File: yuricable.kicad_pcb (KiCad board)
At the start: 2 copper layers, 66 x 25.4 mm, 24 parts, among them U1 FlipperZero

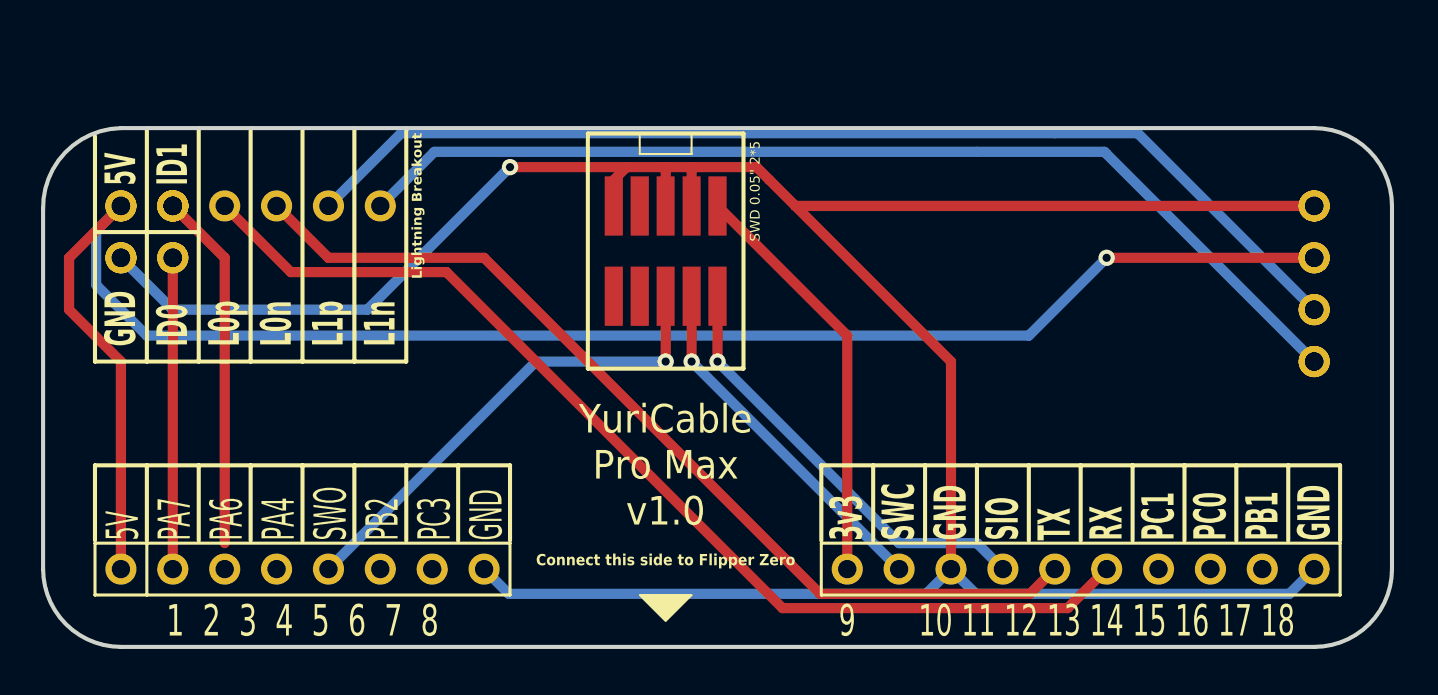
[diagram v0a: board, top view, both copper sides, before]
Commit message: some more markers on silkscreen
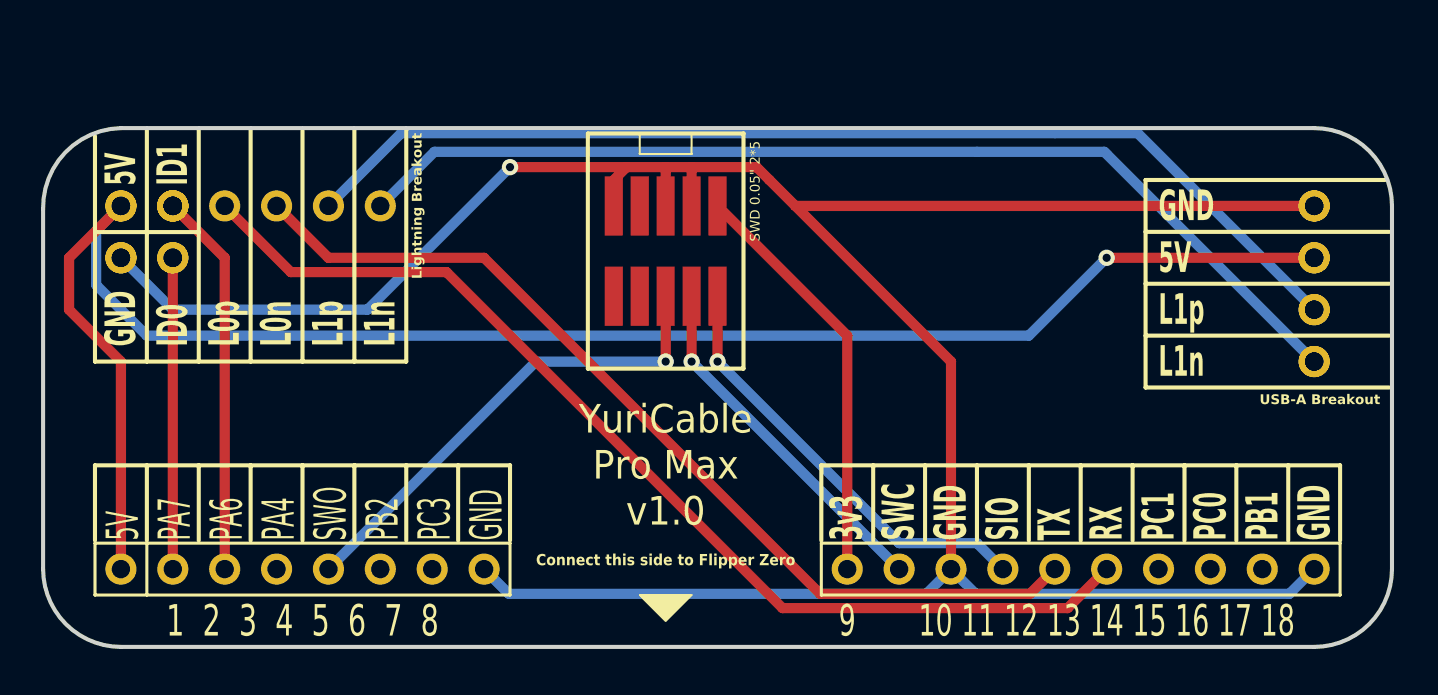
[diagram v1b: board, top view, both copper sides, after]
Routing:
- net /PA6: track 17.6 -> 18.8 mm
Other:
- board text added: "USB-A Breakout"
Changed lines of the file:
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@@
     (grid_origin 91.44 63.5)
     (pcbplotparams
-      (layerselection 0x00010fc_ffffffff)
+      (layerselection 0x003ffff_ffffffff)
       (plot_on_all_layers_selection 0x0000000_00000000)
       (disableapertmacros false)
@@
       (drillshape 0)
       (scaleselection 1)
-      (outputdirectory "gerbers")
+      (outputdirectory "/Users/antonstadie/Developer/KiCAD/yuricable-pcb-kicad/gerber")
     )
   )
@@
   (gr_line (start 62.23 71.12) (end 62.23 74.8)
     (stroke (width 0.2) (type solid)) (layer "F.SilkS"))
+  (gr_line (start 113.665 62.23) (end 125.6 62.23)
+    (stroke (width 0.2) (type solid)) (layer "F.SilkS"))
+  (gr_line (start 113.665 67.31) (end 125.6 67.31)
+    (stroke (width 0.2) (type solid)) (layer "F.SilkS"))
   (gr_line (start 115.57 71.12) (end 115.57 74.8)
     (stroke (width 0.2) (type solid)) (layer "F.SilkS"))
@@
   (gr_line (start 97.79 71.12) (end 97.79 74.8)
     (stroke (width 0.2) (type solid)) (layer "F.SilkS"))
+  (gr_line (start 113.665 64.77) (end 125.6 64.77)
+    (stroke (width 0.2) (type solid)) (layer "F.SilkS"))
   (gr_line (start 64.77 71.12) (end 64.77 74.8)
     (stroke (width 0.2) (type solid)) (layer "F.SilkS"))
@@
     (stroke (width 0.2) (type solid)) (layer "F.SilkS"))
   (gr_line (start 107.95 71.12) (end 107.95 74.8)
+    (stroke (width 0.2) (type solid)) (layer "F.SilkS"))
+  (gr_line (start 113.665 67.31) (end 113.665 57.15)
     (stroke (width 0.2) (type solid)) (layer "F.SilkS"))
   (gr_line (start 118.11 71.12) (end 118.11 74.8)
@@
     )
     (stroke (width 0.1) (type solid)) (fill solid) (layer "F.SilkS"))
+  (gr_line (start 113.665 59.69) (end 125.6 59.69)
+    (stroke (width 0.2) (type solid)) (layer "F.SilkS"))
   (gr_line (start 62.23 59.7) (end 67.31 59.7)
     (stroke (width 0.2) (type solid)) (layer "F.SilkS"))
   (gr_line (start 110.49 71.12) (end 110.49 74.8)
+    (stroke (width 0.2) (type solid)) (layer "F.SilkS"))
+  (gr_line (start 113.665 57.15) (end 125.4 57.15)
     (stroke (width 0.2) (type solid)) (layer "F.SilkS"))
   (gr_line (start 62.23 55) (end 62.23 66.04)
@@
     (effects (font (size 1.5 0.8) (thickness 0.2) bold) (justify left))
   )
+  (gr_text "5V" (at 114.3 60.96) (layer "F.SilkS")
+    (effects (font (size 1.5 0.8) (thickness 0.2) bold) (justify left))
+  )
   (gr_text "Connect this side to Flipper Zero\n\n" (at 90.17 76.2) (layer "F.SilkS")
     (effects (font (size 0.55 0.5) (thickness 0.12) bold))
   )
+  (gr_text "GND" (at 114.3 58.42) (layer "F.SilkS")
+    (effects (font (size 1.5 0.8) (thickness 0.2) bold) (justify left))
+  )
   (gr_text "L1p\n" (at 73.66 65.3 90) (layer "F.SilkS")
+    (effects (font (size 1.5 0.8) (thickness 0.2) bold) (justify left))
+  )
+  (gr_text "L1n" (at 114.3 66.04) (layer "F.SilkS")
     (effects (font (size 1.5 0.8) (thickness 0.2) bold) (justify left))
   )
@@
     (effects (font (size 1.5 0.8) (thickness 0.2) bold) (justify left))
   )
+  (gr_text "USB-A Breakout" (at 122.2 67.9) (layer "F.SilkS")
+    (effects (font (size 0.48 0.48) (thickness 0.12) bold))
+  )
   (gr_text "L0n\n" (at 71.12 65.3 90) (layer "F.SilkS")
+    (effects (font (size 1.5 0.8) (thickness 0.2) bold) (justify left))
+  )
+  (gr_text "L1p" (at 114.3 63.5) (layer "F.SilkS")
     (effects (font (size 1.5 0.8) (thickness 0.2) bold) (justify left))
   )
@@
   (segment (start 83.82 66.04) (end 90.17 66.04) (width 0.5) (layer "B.Cu") (net 13))
   (segment (start 68.58 60.96) (end 66.04 58.42) (width 0.5) (layer "F.Cu") (net 15))
-  (segment (start 68.58 74.93) (end 68.58 60.96) (width 0.5) (layer "F.Cu") (net 15))
+  (segment (start 68.58 60.96) (end 68.58 76.2) (width 0.5) (layer "F.Cu") (net 15))
   (segment (start 66.04 76.2) (end 66.04 60.96) (width 0.5) (layer "F.Cu") (net 16))
 )

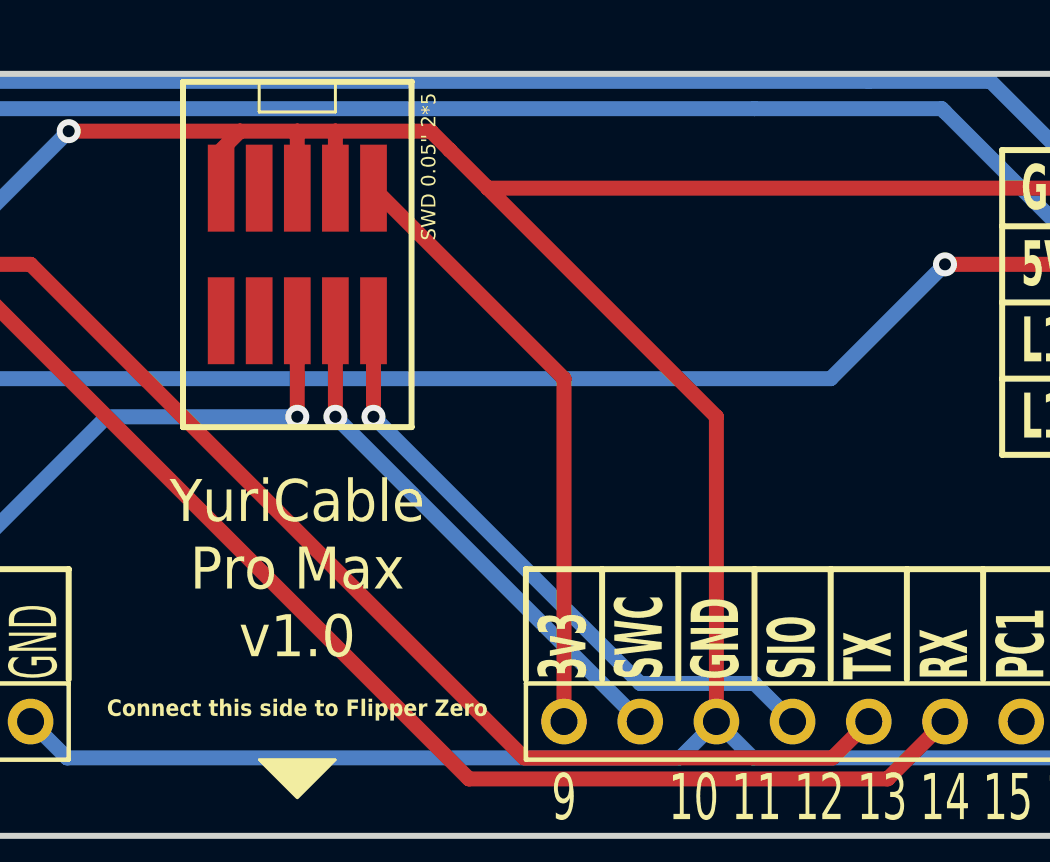
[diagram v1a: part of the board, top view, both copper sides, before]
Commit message: updated Skinny SWD SMT Footprint added Logo to PCB Bumped Revision to v1.1
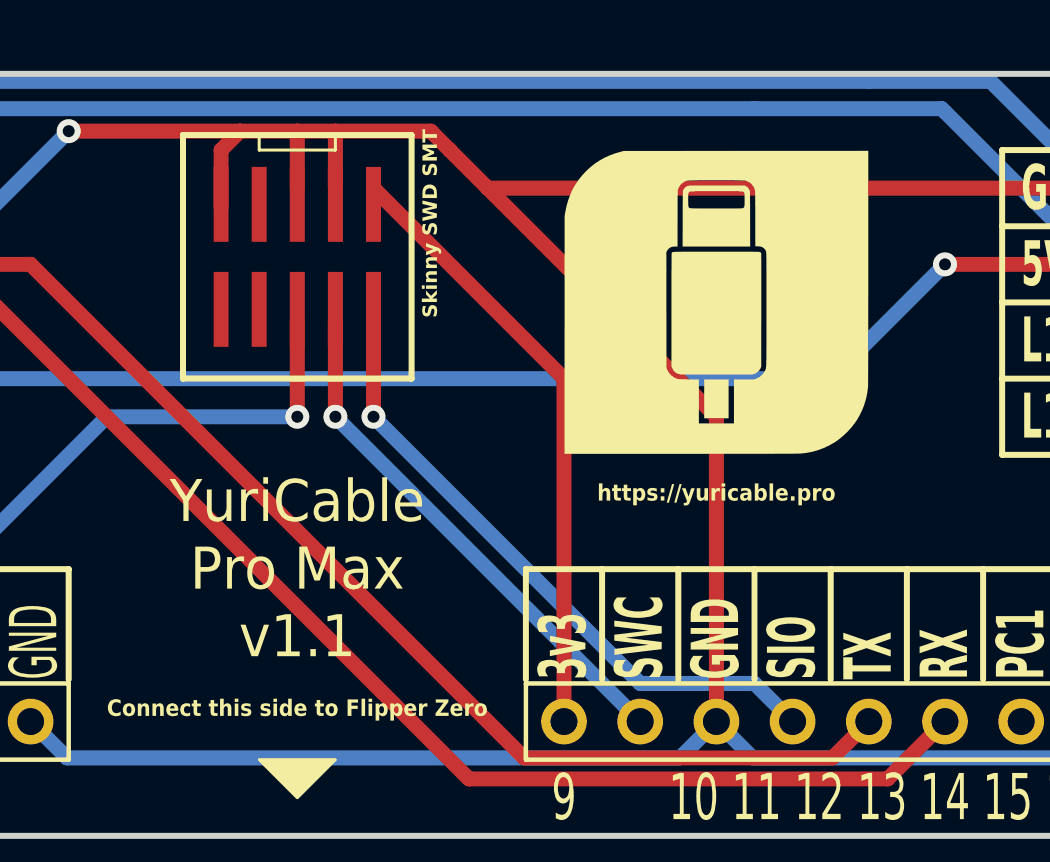
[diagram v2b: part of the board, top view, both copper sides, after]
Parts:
- removed SWD 0.05" 2*5: SWD_0.05_2x5, ARM-JTAG-SWD:SWD_0.05_2x5
- added G***: https://yuricable.pro, YuriCable:YuriCableProMaxLogo, F.Cu at (104.1, 62.2)
- added Skinny SWD SMT: Adafruit 4048 Skinny SWD SMT, ARM-JTAG-SWD:Adafruit 4048 Skinny SWD SMT, F.Cu at (90.2, 61.0)
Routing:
- net GND: track 131.4 -> 133.3 mm
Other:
- board text added: "YuriCable Pro Max v1.1"
- board text added: "https://yuricable.pro"
- board text removed: "YuriCable Pro Max v1.0"

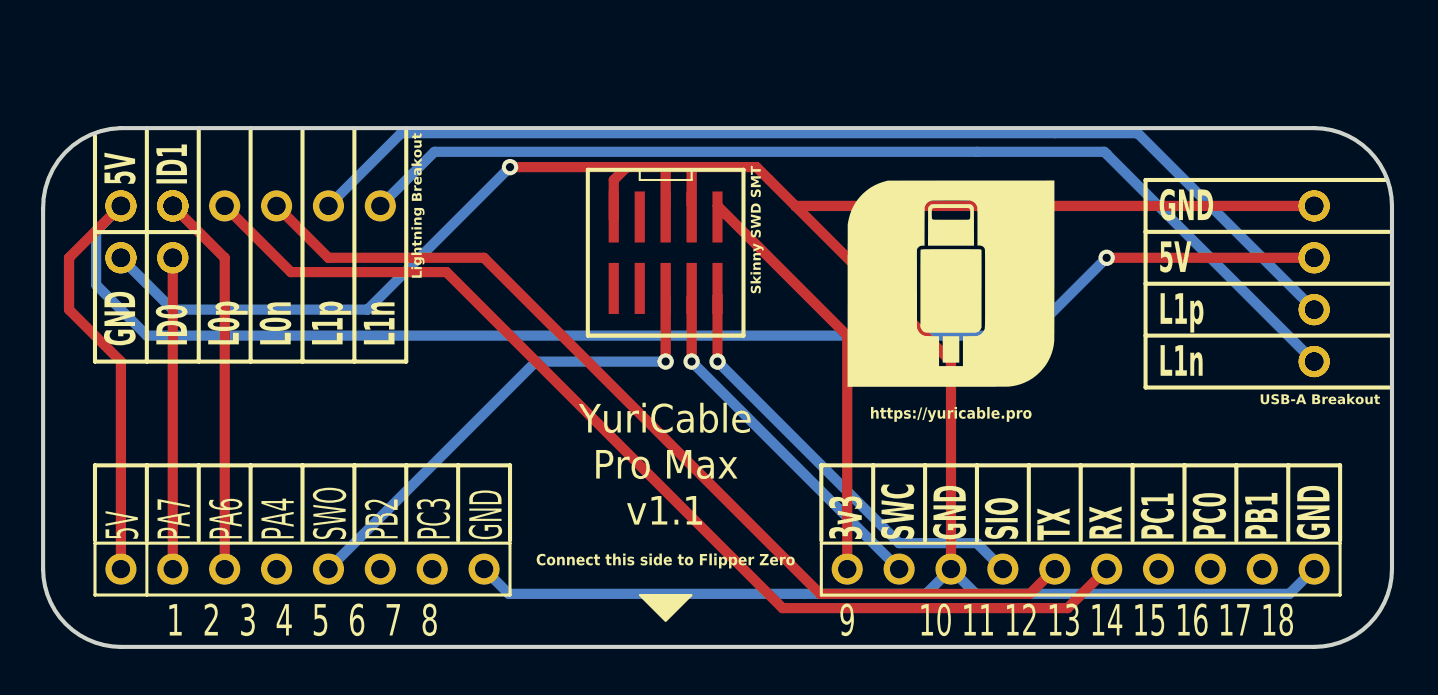
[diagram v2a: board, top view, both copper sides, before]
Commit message: added USB-A female port added logo on backside silkscreen
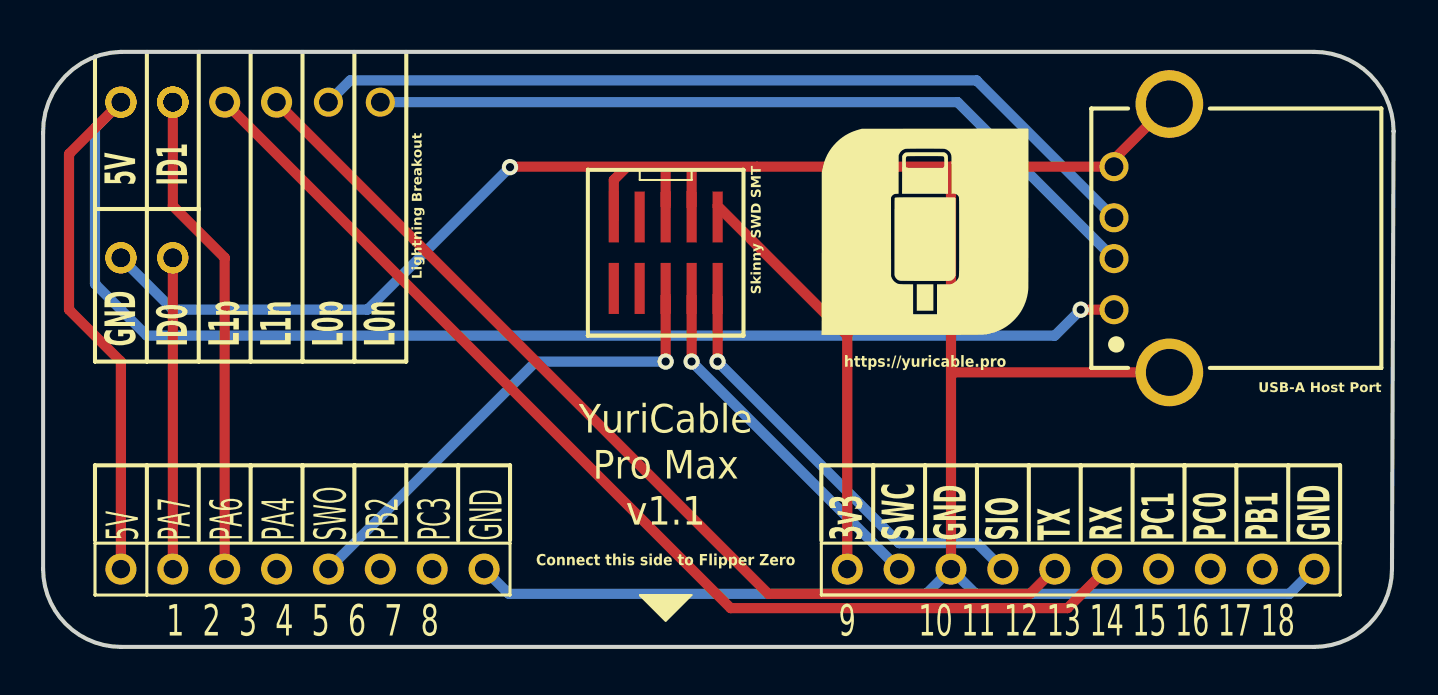
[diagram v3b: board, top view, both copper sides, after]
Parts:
- removed the ? at (121.9, 63.5) (x2)
- removed the ? at (121.9, 66.0) (x2)
- removed the ? at (76.2, 58.4)
- removed the ? at (121.9, 61.0) (x2)
- removed the ? at (73.7, 58.4)
- removed the ? at (121.9, 58.4) (x2)
- added ?: , , F.Cu at (73.7, 53.3)
- added ?: , , F.Cu at (76.2, 53.3)
- added G***: YuriCableProMaxLogoFull, YuriCable:YuriCableProMaxLogoFull, B.Cu at (92.7, 61.0)
- added REF**: 61400416021, USB_Connectors:USB_A_Wuerth_61400416021_Vertical_Right_Angled, F.Cu at (118.1, 60.0)
- moved ? 5.08 mm to (68.6, 53.3)
- moved ? 5.08 mm to (66.0, 53.3) (x4)
- moved ? 5.08 mm to (63.5, 53.3) (x2)
- moved ? 5.08 mm to (71.1, 53.3)
- moved G*** 2.84 mm to (102.9, 59.7)
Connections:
- Skinny SWD SMT pad GND1: (no net) -> GND
- Skinny SWD SMT pad GND2: (no net) -> GND
- Skinny SWD SMT pad GND3: (no net) -> GND
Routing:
- net (no net): track 104.4 -> 0.00 mm
- net /USB+: track 0.00 -> 41.7 mm
- net /USB-: track 0.00 -> 39.1 mm
- net /PA6: track 18.8 -> 23.9 mm
- net GND: track 133.3 -> 136.6 mm
- net /UART_TX: track 46.5 -> 48.6 mm
- net /UART_RX: track 52.1 -> 54.2 mm
- net /5V: track 86.5 -> 85.8 mm
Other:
- board size 66 x 25.4 mm -> 66.1 x 29.1 mm
- board text added: "USB-A Host Port"
- board text removed: "USB-A Breakout"

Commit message: bumped version to v1.2
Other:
- board text added: "YuriCable Pro Max v1.2"
- board text removed: "YuriCable Pro Max v1.1"
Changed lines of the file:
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@@
     )
   )
-  (gr_text "YuriCable \nPro Max \nv1.1" (at 90.17 71.12) (layer "F.SilkS")
+  (gr_text "YuriCable \nPro Max \nv1.2" (at 90.17 71.12) (layer "F.SilkS")
     (effects (font (size 1.4 1.3) (thickness 0.3)))
   )

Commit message: no message
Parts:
- added ? (x4): , , F.Cu at (66.0, 67.3)
- added ? (x4): , , F.Cu at (63.5, 67.3)
- added ? (x2): , , F.Cu at (73.7, 55.9)
- added ? (x4): , , F.Cu at (63.5, 69.8)
- added ?: , , F.Cu at (76.2, 55.9)
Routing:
- net /5V: track 85.8 -> 70.1 mm
- net /USB-: track 39.1 -> 41.6 mm
- net /USB+: track 41.7 -> 44.2 mm
- net /UART_RX: track 54.2 -> 56.3 mm
- net /PA7: track 15.2 -> 16.3 mm
- net /UART_TX: track 48.6 -> 48.5 mm, vias 0 -> 1
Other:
- outline, holes or cut-outs redrawn
